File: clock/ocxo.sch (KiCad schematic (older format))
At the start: 44 parts, among them Q201 MMBT3904, U201 PCA9306, U202 DAC8830, U203 LMV722, U204 LTC2990, U205 LP3853, U206 NC7SZ125, U207 NC7SZ125, Y201 FVXO-HC53, Y202 cx210

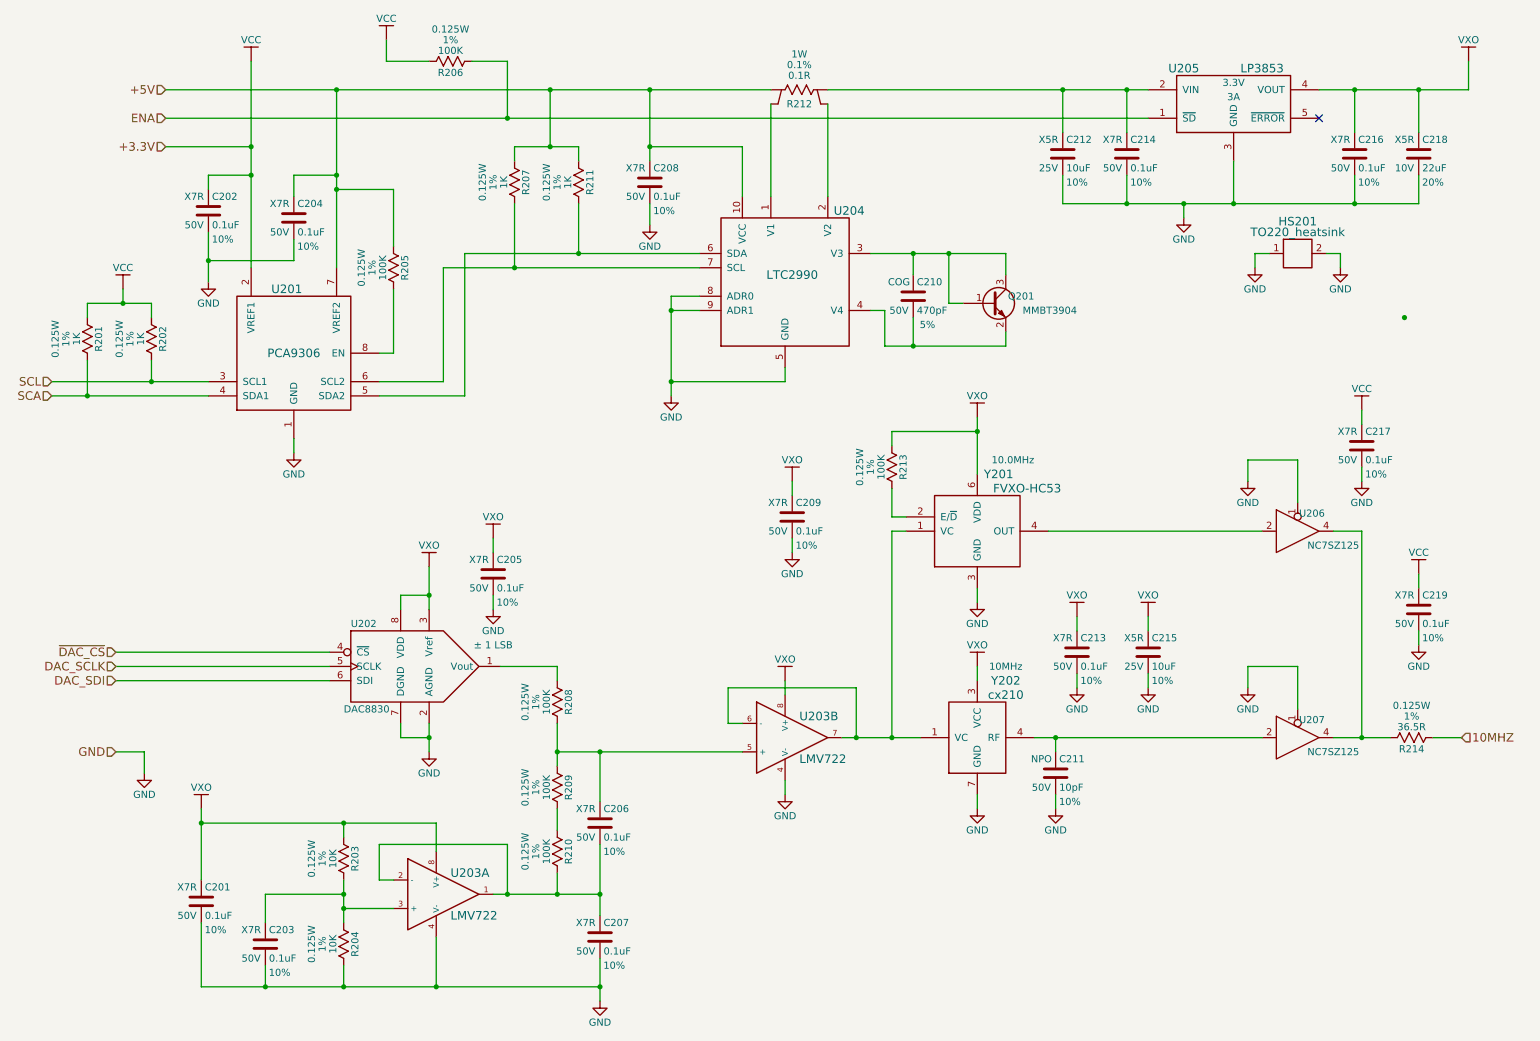
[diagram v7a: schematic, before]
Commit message: Make component parameters consistent for BOM.
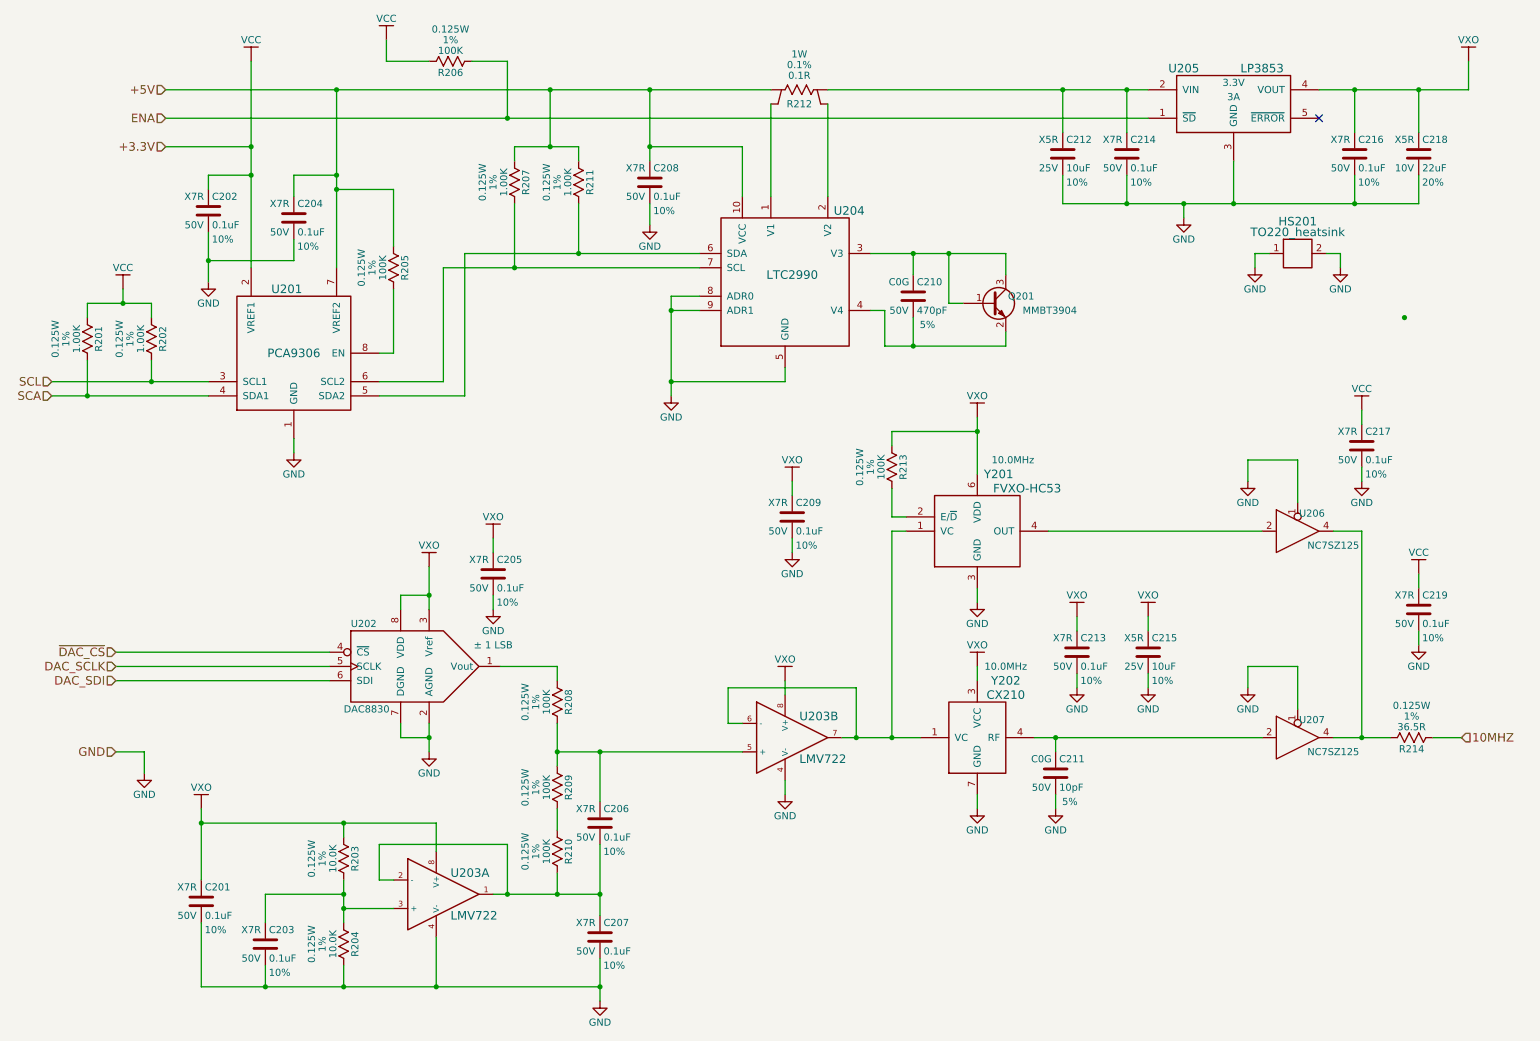
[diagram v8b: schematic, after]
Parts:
- removed Y202: cx210, local:CX210_HandSoldering, symbol cx210
- added Y202: CX210, local:CX210_HandSoldering, symbol CX210
- C210: Dielectric COG -> C0G
- C211: Dielectric NPO -> C0G; PartNum C0805C104K5RACTU -> C0805C100J5GACTU; Tolerance 10% -> 5%
- R201, R202, R207, R211: value 1K -> 1.00K
- R203, R204: value 10K -> 10.0K
- R214: PartNum CRCW0805100KFKEA -> CRCW080536R5FKEA
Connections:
- net GND: now also Y202.7 (GND)
- net VXO: now also Y202.3 (VCC)
- net at U203.6 (-), U203.7, Y201.1 (VC): now also Y202.1 (VC)
- net at C211.1, U207.2: now also Y202.4 (RF)
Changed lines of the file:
@@
 P 2900 6550
 F 0 "R203" V 2980 6550 50  0000 C CNN
-F 1 "10K" V 2825 6550 50  0000 C CNN
+F 1 "10.0K" V 2825 6550 50  0000 C CNN
 F 2 "Resistors_SMD:R_0805_HandSoldering" V 2830 6550 30  0001 C CNN
 F 3 "" V 2980 6550 30  0000 C CNN
@@
 P 2900 7150
 F 0 "R204" V 2980 7150 50  0000 C CNN
-F 1 "10K" V 2825 7150 50  0000 C CNN
+F 1 "10.0K" V 2825 7150 50  0000 C CNN
 F 2 "Resistors_SMD:R_0805_HandSoldering" V 2830 7150 30  0001 C CNN
 F 3 "" V 2980 7150 30  0000 C CNN
@@
 F 3 "" H 7900 5950 60  0000 C CNN
 F 4 "50V" H 7800 5850 50  0000 C CNN "Voltage"
-F 5 "10%" H 8000 5750 50  0000 C CNN "Tolerance"
-F 6 "NPO" H 7800 6050 50  0000 C CNN "Dielectric"
+F 5 "5%" H 8000 5750 50  0000 C CNN "Tolerance"
+F 6 "C0G" H 7800 6050 50  0000 C CNN "Dielectric"
 F 7 "Kemet" H 7900 5950 50  0001 C CNN "Manufacturer"
-F 8 "C0805C104K5RACTU" H 7900 5950 50  0001 C CNN "PartNum"
+F 8 "C0805C100J5GACTU" H 7900 5950 50  0001 C CNN "PartNum"
 	1    7900 5950
 	1    0    0    -1
@@
 F 5 "0.125W" V 10175 5700 50  0000 C CNN "Power"
 F 6 "Vishay Dale" V 10400 5700 50  0001 C CNN "Manufacturer"
-F 7 "CRCW0805100KFKEA" V 10550 5700 50  0001 C CNN "PartNum"
+F 7 "CRCW080536R5FKEA" V 10550 5700 50  0001 C CNN "PartNum"
 	1    10400 5700
 	0    1    1    0
@@
 P 1100 2900
 F 0 "R201" V 1180 2900 50  0000 C CNN
-F 1 "1K" V 1025 2900 50  0000 C CNN
+F 1 "1.00K" V 1025 2900 50  0000 C CNN
 F 2 "Resistors_SMD:R_0805_HandSoldering" V 1030 2900 30  0001 C CNN
 F 3 "" V 1180 2900 30  0000 C CNN
@@
 P 1550 2900
 F 0 "R202" V 1630 2900 50  0000 C CNN
-F 1 "1K" V 1475 2900 50  0000 C CNN
+F 1 "1.00K" V 1475 2900 50  0000 C CNN
 F 2 "Resistors_SMD:R_0805_HandSoldering" V 1480 2900 30  0001 C CNN
 F 3 "" V 1630 2900 30  0000 C CNN
@@
 F 4 "50V" H 6800 2500 50  0000 C CNN "Voltage"
 F 5 "5%" H 7000 2400 50  0000 C CNN "Tolerance"
-F 6 "COG" H 6800 2700 50  0000 C CNN "Dielectric"
+F 6 "C0G" H 6800 2700 50  0000 C CNN "Dielectric"
 F 7 "Kemet" H 6900 2600 50  0001 C CNN "Manufacturer"
 F 8 "C0805C471J5GACTU" H 6900 2600 50  0001 C CNN "PartNum"
@@
 $EndComp
 $Comp
-L cx210 Y202
-U 1 1 563D9183
-P 7350 5700
-F 0 "Y202" H 7550 6100 60  0000 C CNN
-F 1 "cx210" H 7550 6000 60  0000 C CNN
-F 2 "local:CX210_HandSoldering" H 7350 5700 60  0001 C CNN
-F 3 "" H 7500 6100 60  0000 C CNN
-F 4 "10MHz" H 7550 6200 50  0000 C CNN "Frequency"
-F 5 "Connor Winfield" H 7550 6375 50  0001 C CNN "Manufacturer"
-F 6 "OH300-50503CV-010.0M" H 7550 6300 50  0001 C CNN "PartNum"
-	1    7350 5700
-	1    0    0    -1
-$EndComp
-$Comp
 L R_local R207
 U 1 1 5640052F
 P 4100 1800
 F 0 "R207" V 4180 1800 50  0000 C CNN
-F 1 "1K" V 4025 1800 50  0000 C CNN
+F 1 "1.00K" V 4025 1800 50  0000 C CNN
 F 2 "Resistors_SMD:R_0805_HandSoldering" V 4030 1800 30  0001 C CNN
 F 3 "" V 4180 1800 30  0000 C CNN
@@
 P 4550 1800
 F 0 "R211" V 4630 1800 50  0000 C CNN
-F 1 "1K" V 4475 1800 50  0000 C CNN
+F 1 "1.00K" V 4475 1800 50  0000 C CNN
 F 2 "Resistors_SMD:R_0805_HandSoldering" V 4480 1800 30  0001 C CNN
 F 3 "" V 4630 1800 30  0000 C CNN
@@
 Connection ~ 4350 1150
 Connection ~ 10350 2750
+$Comp
+L CX210 Y202
+U 1 1 563F1575
+P 7350 5700
+F 0 "Y202" H 7550 6100 60  0000 C CNN
+F 1 "CX210" H 7550 6000 60  0000 C CNN
+F 2 "local:CX210_HandSoldering" H 7350 5700 60  0001 C CNN
+F 3 "" H 7500 6100 60  0000 C CNN
+F 4 "10.0MHz" H 7550 6200 50  0000 C CNN "Frequency"
+F 5 "Connor Winfield" H 7550 6375 50  0001 C CNN "Manufacturer"
+F 6 "OH300-50503CV-010.0M" H 7550 6300 50  0001 C CNN "PartNum"
+	1    7350 5700
+	1    0    0    -1
+$EndComp
 $EndSCHEMATC
